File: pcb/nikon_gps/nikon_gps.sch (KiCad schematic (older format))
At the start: 42 parts, among them J1 1x03 pads, Q1 NMOS, SW1 ON/OFF, U1 Hornet ORG1411, U2 74AUP1T08, U3 SN74LV1T126, U4 TPS62203DBV, U5 74LVC1G14

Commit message: Update.
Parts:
- C1: value 100nF -> 1uF
- C6: value 1nF -> 10nF
- C8: value 100nF -> 2.2uF
- D1: value Shottky -> RB521S30T5G
- Q1: value NMOS -> 2N7002WT1G; Mfr (none) -> ON Semi
- R10: value 330 -> 470
- R3, R4: value 10K -> 33K
- R5: value 22K -> 33K
- R8: value 4.7K -> 1K
- R9: value 33K -> 1K
- U2: value 74AUP1T08 -> SN74AUP1T08DCKR
- U3: value SN74LV1T126 -> SN74LV1T126DBVR
- U4: value TPS62203DBV -> TPS62203DBVR
- U5: value 74LVC1G14 -> SN74LVC1G14DBVR
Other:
- note added: "Low Vf diode"
- note added: "On/off LEDs"
- note removed: "On/off\nLEDs"
- moved on the sheet: C10, C3, D2, D3, Q1, R10, R11, R4, R5, R9, U2

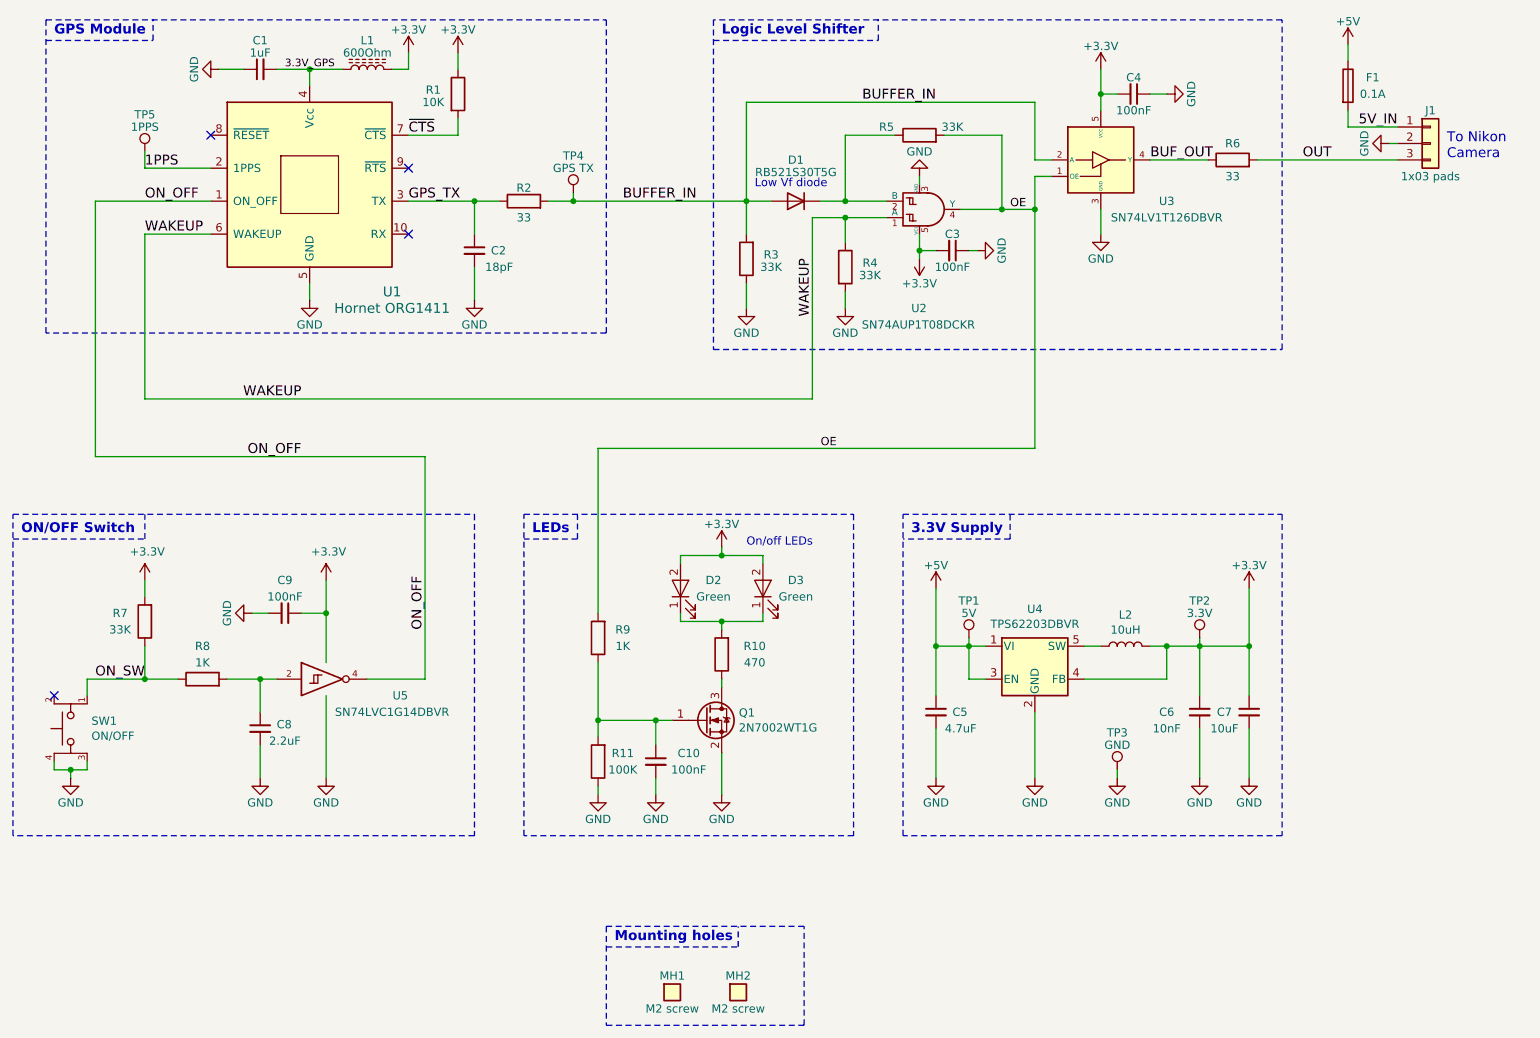
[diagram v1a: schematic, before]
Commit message: 1. PCB update. 2. Updated 3D model images.
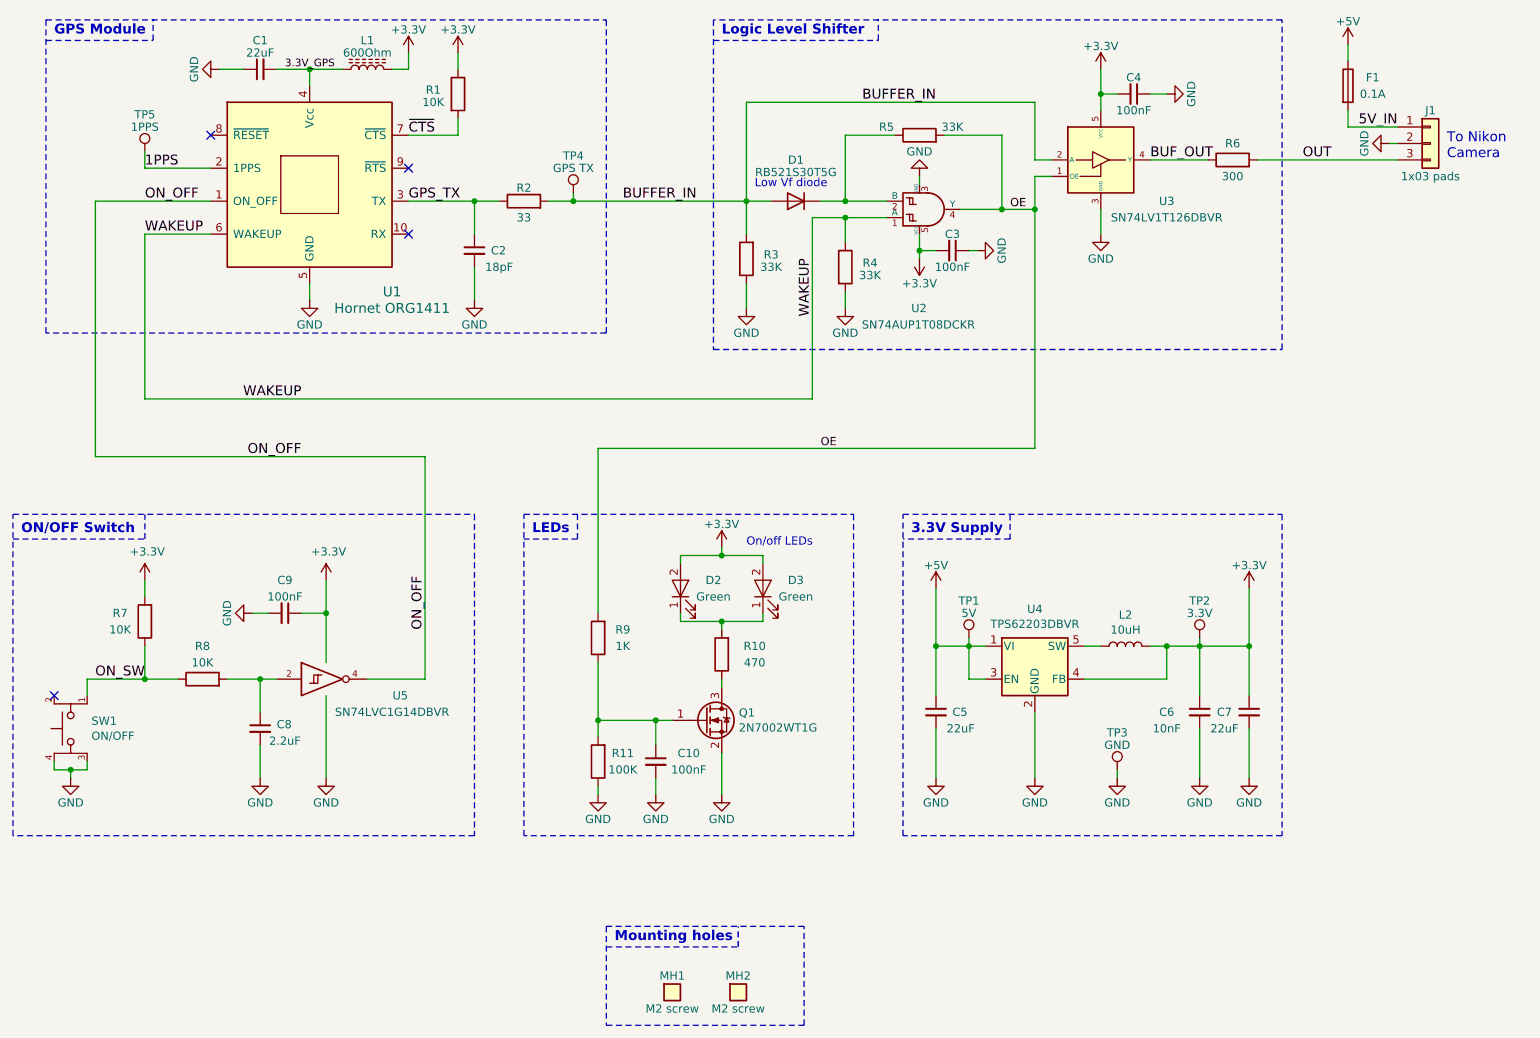
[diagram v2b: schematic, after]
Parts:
- C1: value 1uF -> 22uF
- C5: value 4.7uF -> 22uF
- C7: value 10uF -> 22uF; PN (none) -> CL21A226MPCLRNC
- Q1: PN (none) -> 2N7002BKW,115
- R6: value 33 -> 300
- R7: value 33K -> 10K
- R8: value 1K -> 10K
